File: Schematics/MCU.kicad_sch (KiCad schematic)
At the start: 27 parts, among them J1 Microsemi_FlashPro-JTAG-10, U3 STM32F405RGT6, Y1 8mhz

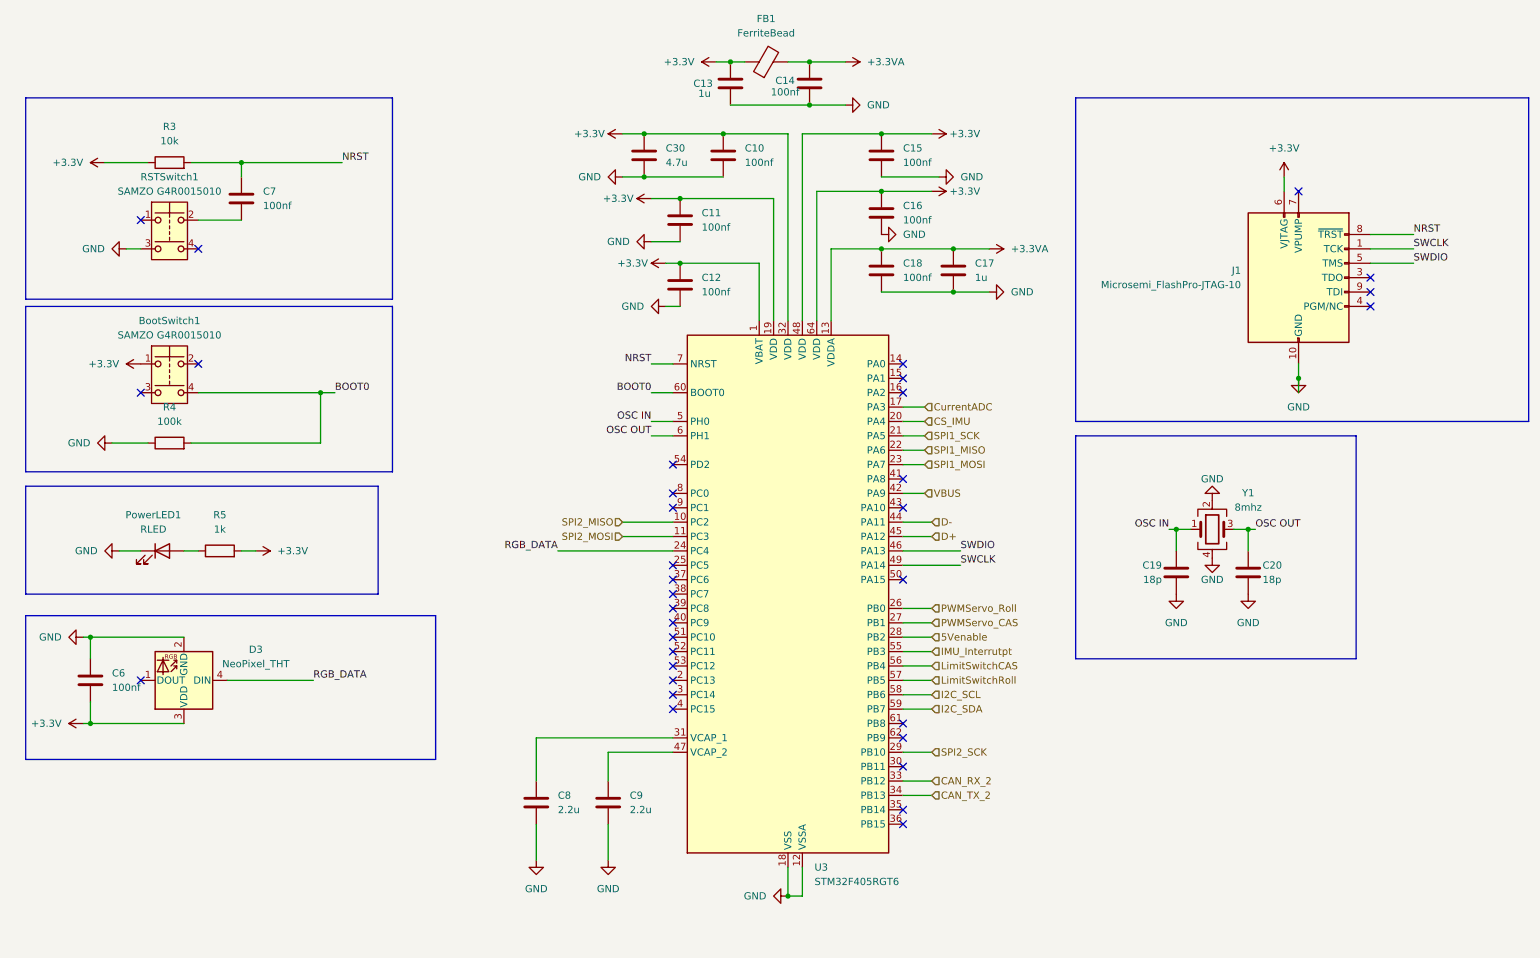
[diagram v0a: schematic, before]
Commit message: started new design with esp32
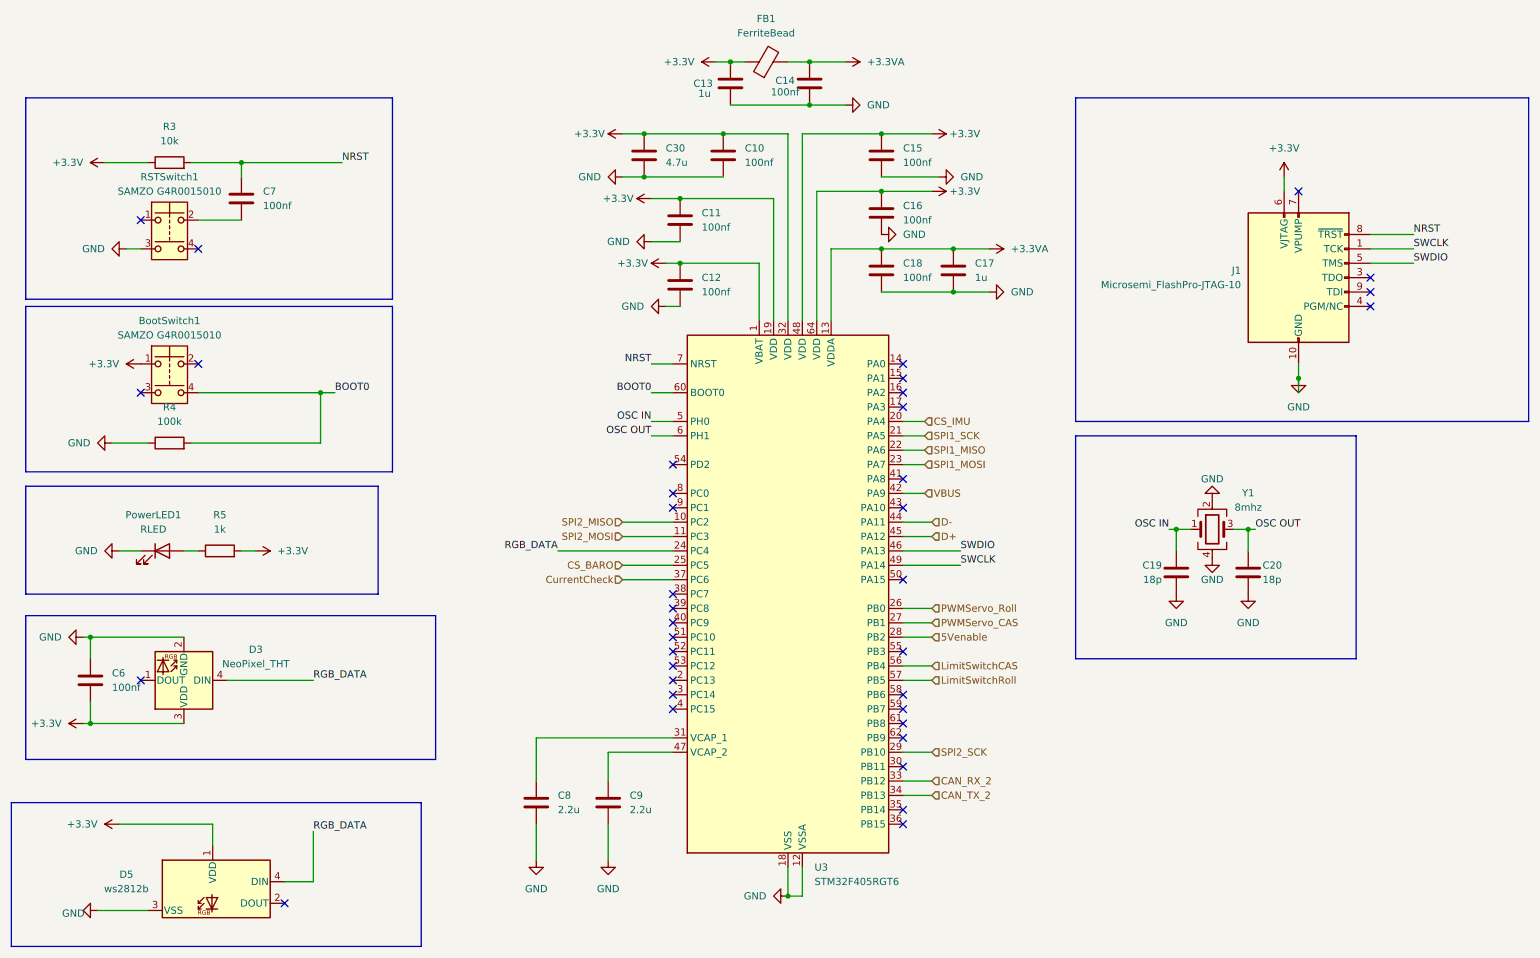
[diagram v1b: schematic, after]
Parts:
- added D5: ws2812b, LED_SMD:LED_WS2812B_PLCC4_5.0x5.0mm_P3.2mm, symbol LED:NeoPixel_THT
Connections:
- net +3.3V: now also D5.1 (VDD)
- net GND: now also D5.3 (VSS)
- net RGB_DATA: now also D5.4 (DIN)
- net CS_BARO: now reaches U3.25 (PC5)
- net CurrentCheck: now reaches U3.37 (PC6)
- net CurrentADC: no longer names the net of U3.17 (PA3)
- net I2C_SCL: no longer names the net of U3.58 (PB6)
- net I2C_SDA: no longer names the net of U3.59 (PB7)
- net IMU_Interrutpt: no longer names the net of U3.55 (PB3)
- no-connect marks 34 -> 37

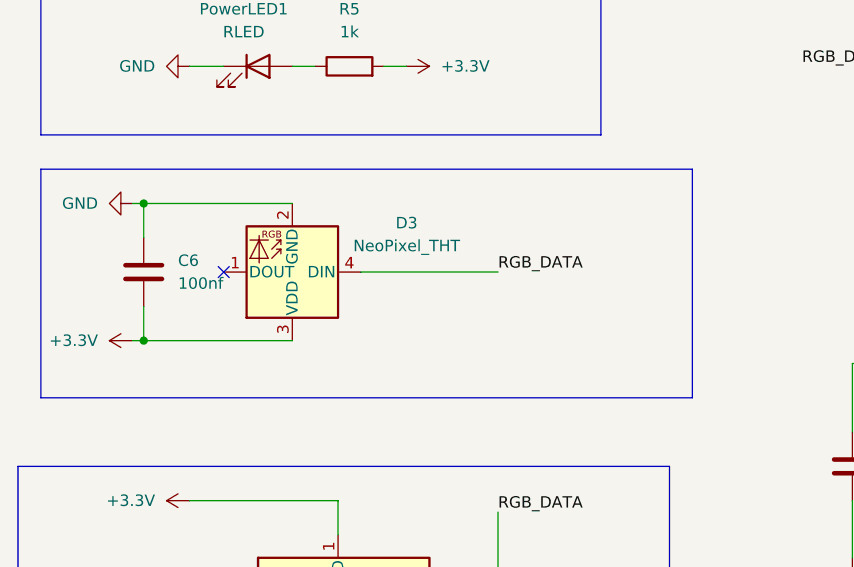
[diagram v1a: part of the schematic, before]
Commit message: added esp32 for uart to tune control systems from a web browser app
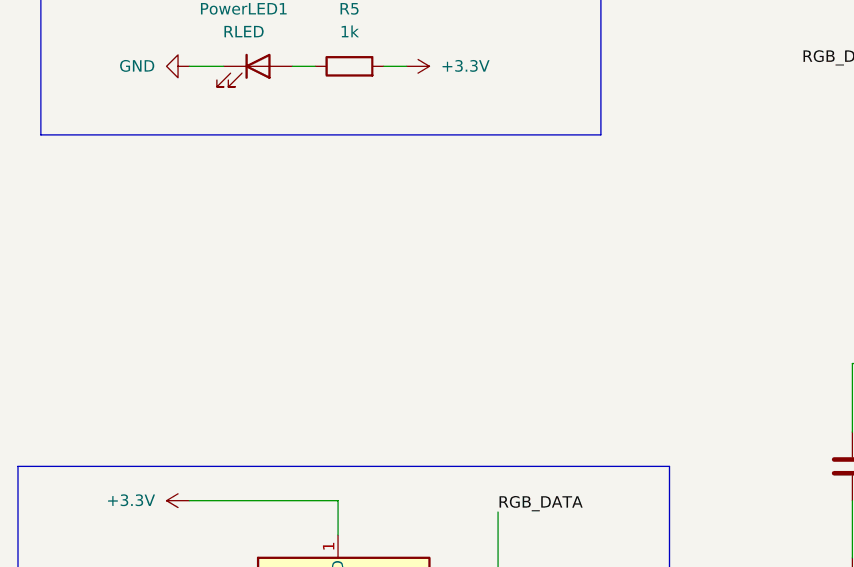
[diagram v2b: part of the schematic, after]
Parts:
- removed C6: 100nf, Capacitor_SMD:C_0805_2012Metric_Pad1.18x1.45mm_HandSolder, symbol Device:C
- removed D3: NeoPixel_THT, LED_SMD:LED_Kingbright_AAA3528ESGCT, symbol LED:NeoPixel_THT
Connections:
- no-connect marks 37 -> 36

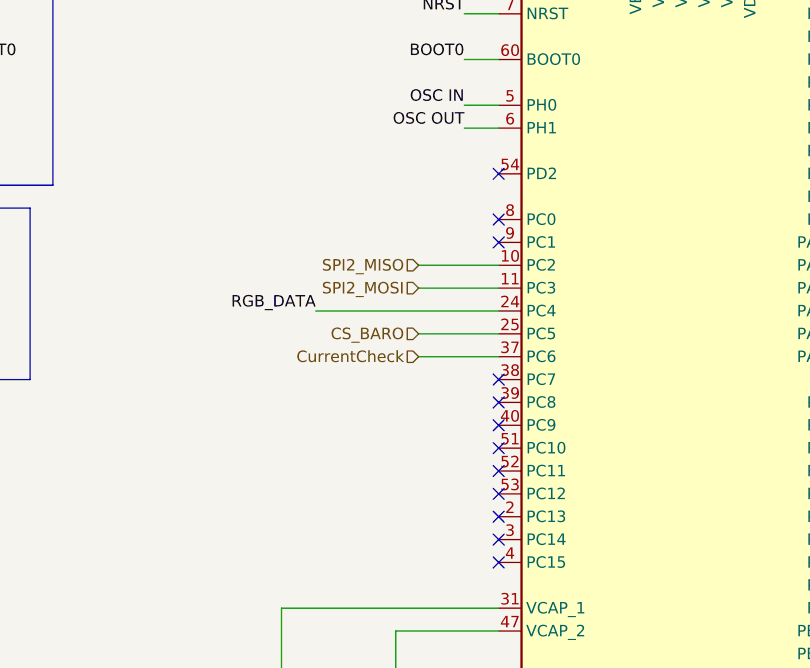
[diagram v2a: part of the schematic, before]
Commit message: clean up of routing
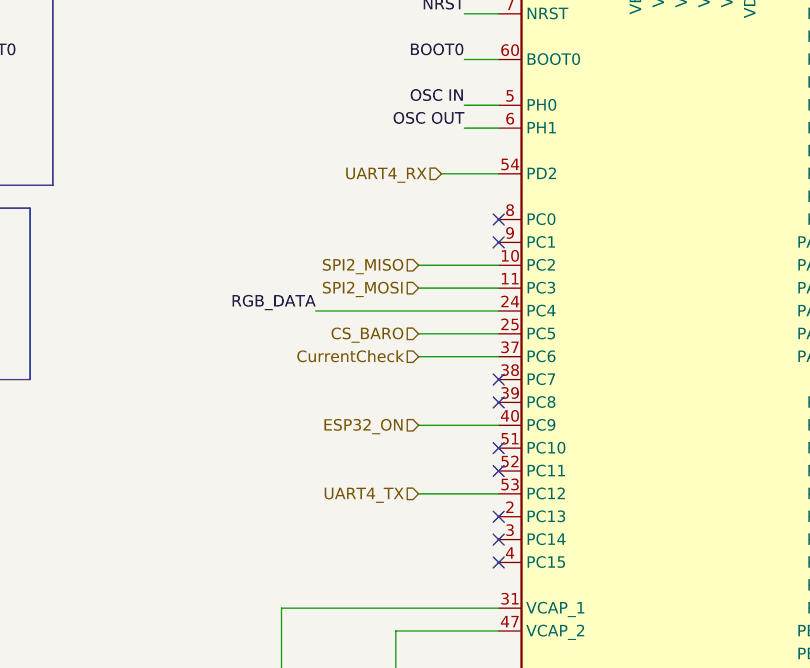
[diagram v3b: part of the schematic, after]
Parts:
- C30: LCSC (none) -> C98192
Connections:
- net ESP32_ON: now reaches U3.40 (PC9)
- net UART4_TX: now reaches U3.53 (PC12)
- net UART4_RX: now reaches U3.54 (PD2)
- no-connect marks 36 -> 33
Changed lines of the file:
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@@
+	)
+	(no_connect
+		(at 172.72 78.74)
 	)
 	(no_connect
@@
 	)
 	(no_connect
-		(at 132.08 93.98)
-	)
-	(no_connect
 		(at 132.08 119.38)
 	)
@@
 	)
 	(no_connect
-		(at 132.08 129.54)
-	)
-	(no_connect
 		(at 172.72 101.6)
 	)
@@
 	)
 	(no_connect
-		(at 172.72 78.74)
-	)
-	(no_connect
 		(at 172.72 157.48)
 	)
@@
 	)
 	(no_connect
-		(at 132.08 121.92)
-	)
-	(no_connect
 		(at 132.08 132.08)
 	)
@@
 	(wire
 		(pts
+			(xy 125.73 93.98) (xy 132.08 93.98)
+		)
+		(stroke
+			(width 0)
+			(type default)
+		)
+	)
+	(wire
+		(pts
 			(xy 157.48 45.72) (xy 157.48 68.58)
 		)
@@
 	(wire
 		(pts
+			(xy 123.19 129.54) (xy 132.08 129.54)
+		)
+		(stroke
+			(width 0)
+			(type default)
+		)
+	)
+	(wire
+		(pts
 			(xy 168.91 55.88) (xy 181.61 55.88)
 		)
@@
 		(pts
 			(xy 262.89 53.34) (xy 255.27 53.34)
+		)
+		(stroke
+			(width 0)
+			(type default)
+		)
+	)
+	(wire
+		(pts
+			(xy 123.19 121.92) (xy 132.08 121.92)
 		)
 		(stroke
@@
 		)
 	)
+	(hierarchical_label "UART4_RX"
+		(shape input)
+		(at 125.73 93.98 180)
+		(effects
+			(font
+				(size 1.27 1.27)
+			)
+			(justify right)
+		)
+	)
 	(hierarchical_label "SPI2_SCK"
 		(shape input)
@@
 		)
 	)
+	(hierarchical_label "ESP32_ON"
+		(shape input)
+		(at 123.19 121.92 180)
+		(effects
+			(font
+				(size 1.27 1.27)
+			)
+			(justify right)
+		)
+	)
 	(hierarchical_label "CAN_RX_2"
 		(shape input)
@@
 			)
 			(justify left)
+		)
+	)
+	(hierarchical_label "UART4_TX"
+		(shape input)
+		(at 123.19 129.54 180)
+		(effects
+			(font
+				(size 1.27 1.27)
+			)
+			(justify right)
 		)
 	)
@@
 			)
 		)
-		(property "LCSC" ""
+		(property "LCSC" "C98192"
 			(at 127 39.37 0)
 			(effects

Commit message: updated board waiting on review
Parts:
- added C22: 100nf, Capacitor_SMD:C_0805_2012Metric_Pad1.18x1.45mm_HandSolder, symbol Device:C
- J1: footprint myFootprints:CONN_7024610XX_MOL -> Connector_PinHeader_1.27mm:PinHeader_2x05_P1.27mm_Vertical
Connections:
- net +3.3V: now also C22.1
- net GND: now also C22.2

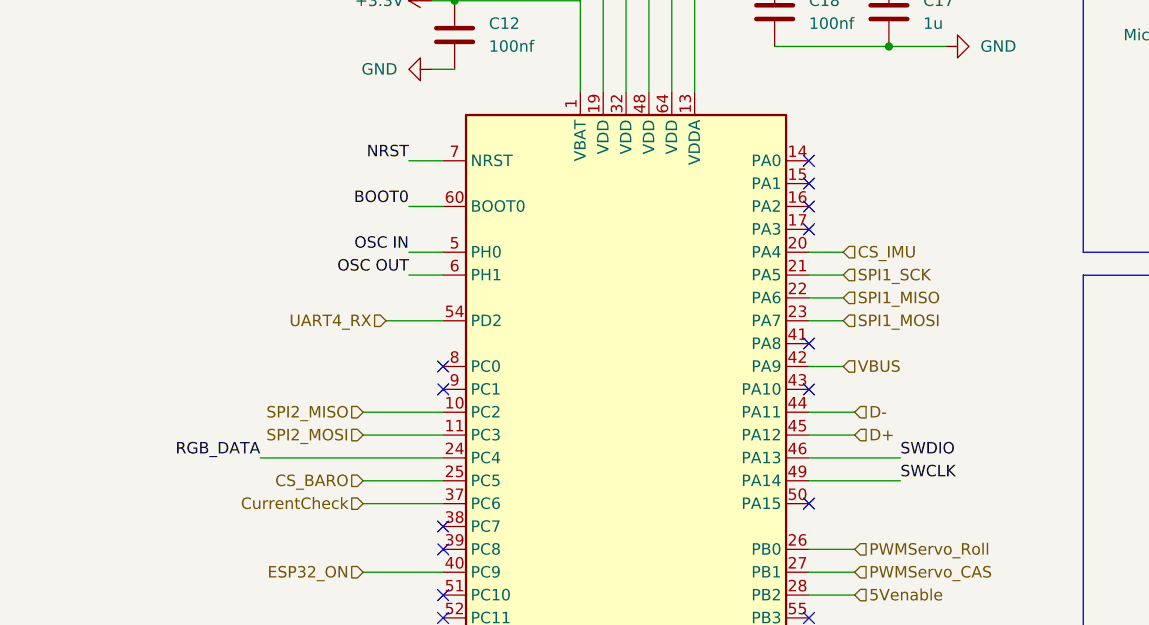
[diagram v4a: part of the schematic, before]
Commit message: Updating to KiCad 10.0
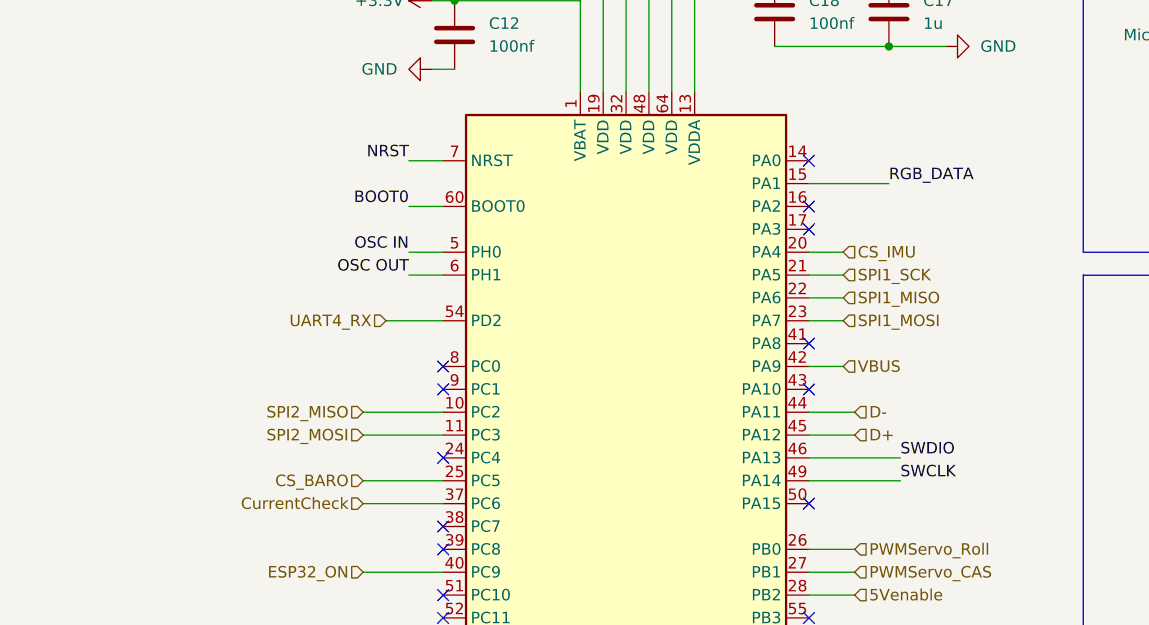
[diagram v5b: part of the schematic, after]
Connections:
- net RGB_DATA: now also U3.15 (PA1); no longer U3.24 (PC4)
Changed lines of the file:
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@@
-	)
-	(no_connect
-		(at 172.72 78.74)
 	)
 	(no_connect
@@
 	)
 	(no_connect
+		(at 132.08 109.22)
+	)
+	(no_connect
 		(at 255.27 63.5)
 	)
@@
 	(wire
 		(pts
+			(xy 181.61 78.74) (xy 172.72 78.74)
+		)
+		(stroke
+			(width 0)
+			(type default)
+		)
+	)
+	(wire
+		(pts
 			(xy 127 35.56) (xy 140.97 35.56)
 		)
@@
 		(pts
 			(xy 176.53 88.9) (xy 172.72 88.9)
-		)
-		(stroke
-			(width 0)
-			(type default)
-		)
-	)
-	(wire
-		(pts
-			(xy 111.76 109.22) (xy 132.08 109.22)
 		)
 		(stroke
@@
 	)
 	(label "RGB_DATA"
-		(at 111.76 109.22 180)
-		(effects
-			(font
-				(size 1.27 1.27)
-			)
-			(justify right bottom)
-		)
-	)
+		(at 181.61 78.74 0)
+		(effects
+			(font
+				(size 1.27 1.27)
+			)
+			(justify left bottom)
+		)
+	)

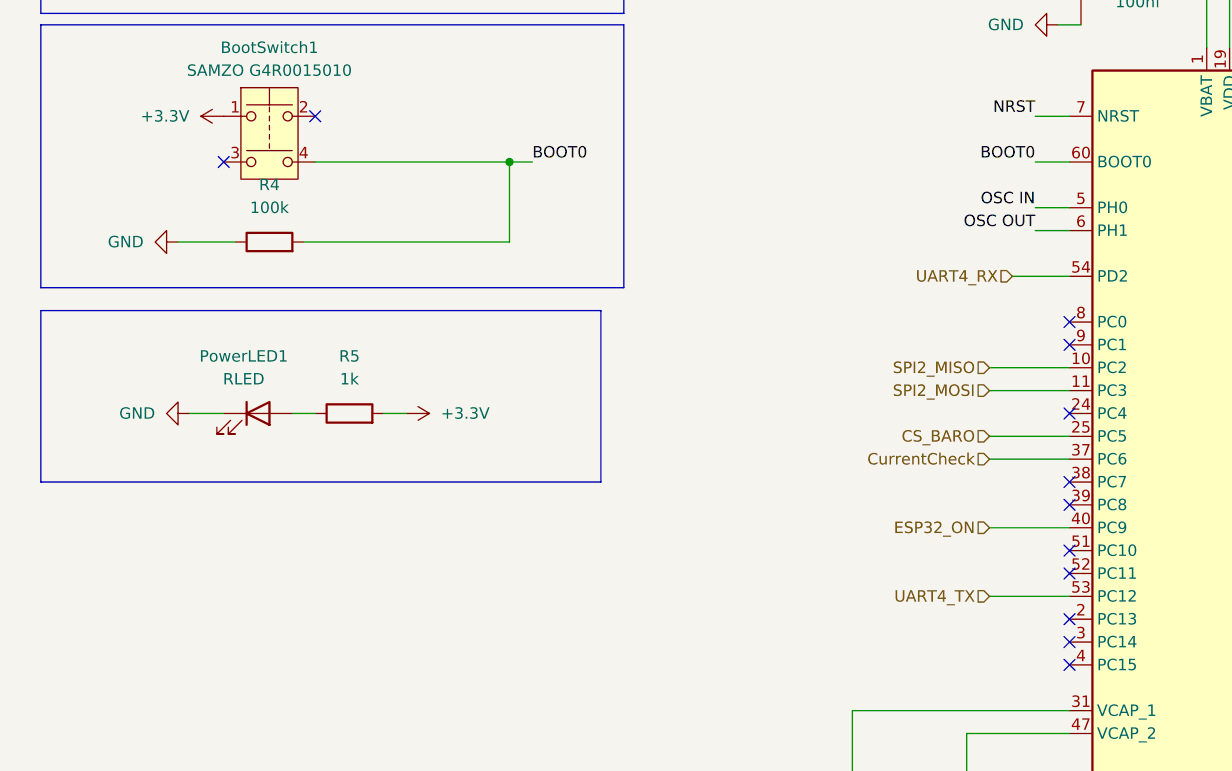
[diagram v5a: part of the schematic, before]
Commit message: removed esp32 to seperate board, added gps breakout, pending final review for purchase
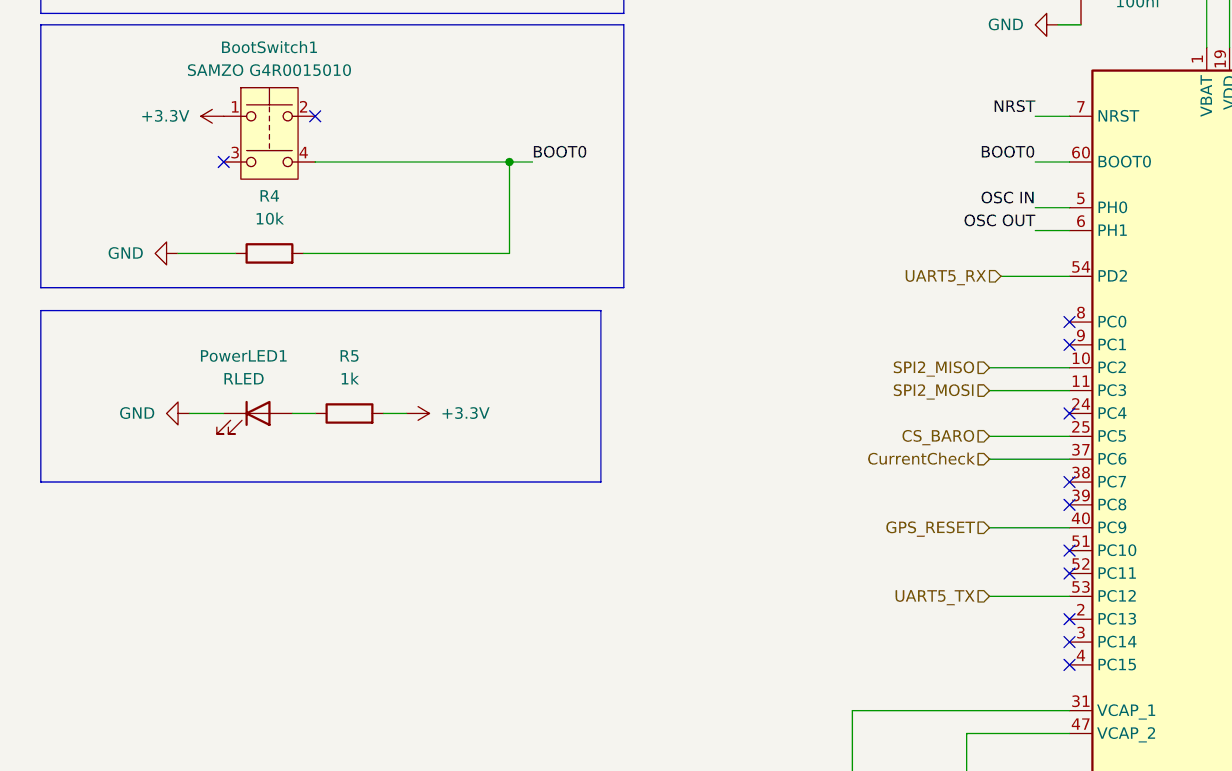
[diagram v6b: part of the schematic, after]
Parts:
- R4: value 100k -> 10k
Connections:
- net ESP32_ON renamed GPS_RESET
- net UART4_RX renamed UART5_RX
- net UART4_TX renamed UART5_TX
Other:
- moved on the sheet: R4

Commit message: final draft, in JLPCB cart
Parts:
- D5: LCSC C114586 -> C2761795
- J1: LCSC C585350 -> C22438120; LCSC Part C585350 -> C22438120
- R4: LCSC C96346 -> C84376
